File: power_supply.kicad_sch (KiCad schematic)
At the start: 27 parts, among them J1 USB_C_Receptacle_USB2.0_16P, J2 B2B-XH-A, J3 USB_C_Receptacle_USB2.0_16P, SW9 SW_SPDT

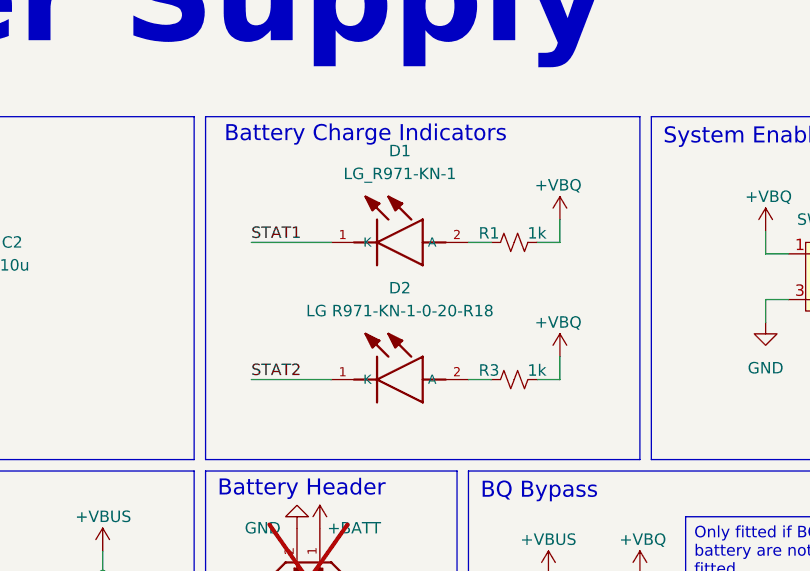
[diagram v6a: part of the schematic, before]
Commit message: refac: changes LED MPN and unfits them
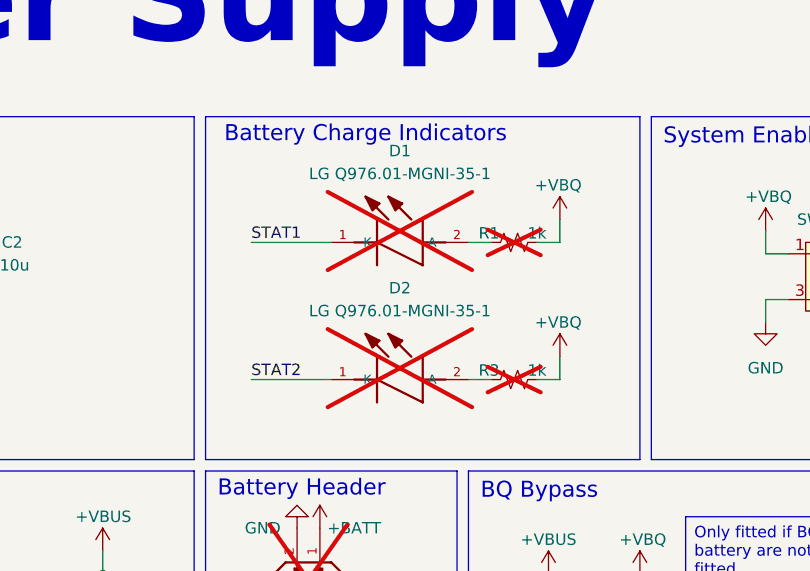
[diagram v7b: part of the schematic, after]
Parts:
- D1: value LG_R971-KN-1 -> LG Q976.01-MGNI-35-1; footprint LG_R971-KN-1:LEDC2012X80N -> LED_SMD:LED_0603_1608Metric; MPN LG R971-KN-1-0-20-R18 -> LG Q976.01-MGNI-35-1; now not fitted
- D2: value LG R971-KN-1-0-20-R18 -> LG Q976.01-MGNI-35-1; footprint LG_R971-KN-1:LEDC2012X80N -> LED_SMD:LED_0603_1608Metric; MPN LG R971-KN-1-0-20-R18 -> LG Q976.01-MGNI-35-1; now not fitted
- R1, R3: now not fitted
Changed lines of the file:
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@@
 		(in_bom yes)
 		(on_board yes)
-		(dnp no)
+		(dnp yes)
 		(property "Reference" "R1"
 			(at 194.056 48.514 90)
@@
 		(in_bom yes)
 		(on_board yes)
-		(dnp no)
+		(dnp yes)
 		(fields_autoplaced yes)
 		(property "Reference" "D2"
@@
 			)
 		)
-		(property "Value" "LG R971-KN-1-0-20-R18"
+		(property "Value" "LG Q976.01-MGNI-35-1"
 			(at 184.15 57.15 0)
 			(effects
@@
 			)
 		)
-		(property "Footprint" "LG_R971-KN-1:LEDC2012X80N"
+		(property "Footprint" "LED_SMD:LED_0603_1608Metric"
 			(at 176.53 64.77 0)
 			(effects
@@
 			)
 		)
-		(property "MPN" "LG R971-KN-1-0-20-R18"
+		(property "MPN" "LG Q976.01-MGNI-35-1"
 			(at 176.53 64.77 0)
 			(effects
@@
 		(in_bom yes)
 		(on_board yes)
-		(dnp no)
+		(dnp yes)
 		(fields_autoplaced yes)
 		(property "Reference" "D1"
@@
 			)
 		)
-		(property "Value" "LG_R971-KN-1"
+		(property "Value" "LG Q976.01-MGNI-35-1"
 			(at 184.15 41.91 0)
 			(effects
@@
 			)
 		)
-		(property "Footprint" "LG_R971-KN-1:LEDC2012X80N"
+		(property "Footprint" "LED_SMD:LED_0603_1608Metric"
 			(at 176.53 49.53 0)
 			(effects
@@
 			)
 		)
-		(property "Datasheet" ""
+		(property "Datasheet" "https://www.digikey.com.br/en/products/detail/ams-osram-usa-inc/LG-Q976-01-MGNI-35-1/21556493"
 			(at 176.53 49.53 0)
 			(effects
@@
 			)
 		)
-		(property "MPN" "LG R971-KN-1-0-20-R18"
+		(property "MPN" "LG Q976.01-MGNI-35-1"
 			(at 176.53 49.53 0)
 			(effects
@@
 		(in_bom yes)
 		(on_board yes)
-		(dnp no)
+		(dnp yes)
 		(property "Reference" "R3"
 			(at 194.056 63.754 90)

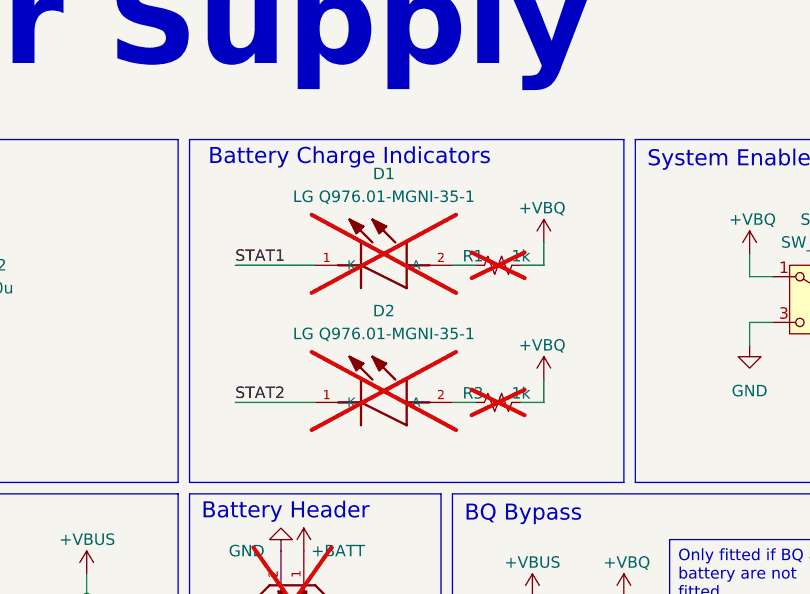
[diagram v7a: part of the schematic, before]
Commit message: feat: adds pin headers
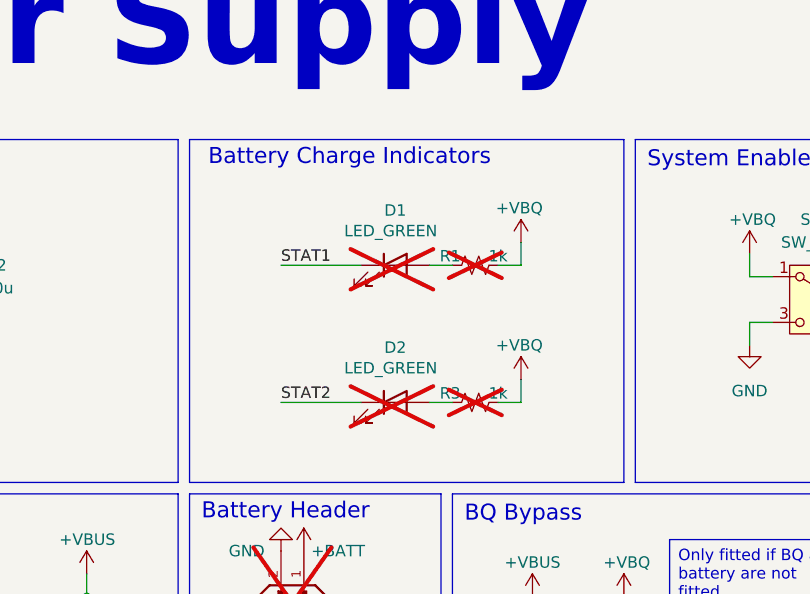
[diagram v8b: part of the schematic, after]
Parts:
- removed D1, D2: LG Q976.01-MGNI-35-1, LED_SMD:LED_0603_1608Metric, symbol LG_R971-KN-1:LG_R971-KN-1
- added D1, D2: LED_GREEN, LED_SMD:LED_0603_1608Metric, symbol Device:LED
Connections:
- net STAT1: now also D1.1 (K)
- net STAT2: now also D2.1 (K)
- net at R1.1: now also D1.2 (A)
- net at R3.1: now also D2.2 (A)
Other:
- moved on the sheet: R1, R3
